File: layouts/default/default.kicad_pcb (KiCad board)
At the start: 2 copper layers, 38 x 75 mm, 52 parts, among them U2 LDO Vin max Iq, U3 LDO Vin max Iq

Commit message: do some layouts
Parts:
- removed C17: , atopile:C_0402_1005Metric
- added C13: 100nF ±10% 16V X7R, atopile:C0402-b3ef17, B.Cu at (0.00, 28.8)
- added C14: 100nF ±10% 16V X7R, atopile:C0402-b3ef17, B.Cu at (0.00, 33.8)
- added C15: 100nF ±10% 16V X7R, atopile:C0402-b3ef17, B.Cu at (0.00, 38.8)
- added C16: 100nF ±10% 16V X7R, atopile:C0402-b3ef17, B.Cu at (0.00, 47.9)
- added LED6: , atopile:LED-SMD_4P-L3.5-W2.8-BR-1-15b4e8, B.Cu at (0.00, 31.0)
- added LED7: , atopile:LED-SMD_4P-L3.5-W2.8-BR-1-15b4e8, B.Cu at (0.00, 36.0)
- added LED8: , atopile:LED-SMD_4P-L3.5-W2.8-BR-1-15b4e8, B.Cu at (0.00, 41.0)
- added LED9: , atopile:LED-SMD_4P-L3.5-W2.8-BR-1-15b4e8, B.Cu at (0.00, 46.0)
- C4, C5: value 100nF ±10% 50V X7R -> 20pF ±5% 50V C0G; footprint atopile:C0603-bd72f6 -> atopile:C0402-b3ef17
- Q1: footprint atopile:SOT-23-3_L2.9-W1.3-P1.90-LS2.4-BL-1-fcaf94 -> atopile:SOT-23-3_L2.9-W1.3-P1.90-LS2.4-BR-688f29
- R5: value 10kΩ ±1% 100mW -> 0Ω 100mW
- moved U4 36.5 mm to (-0.20, 43.5)
- moved S2 33.7 mm to (-21.1, 21.6), turned to -90 degrees
- moved R8 25.6 mm to (-18.7, 23.1)
- moved C1 24.2 mm to (-13.9, -8.60)
- moved C6 23.2 mm to (-17.1, 23.1)
- moved R7 22.1 mm to (-9.10, 9.60), turned to -90 degrees
- moved R12 19.6 mm to (17.6, 21.5), turned to -90 degrees
- moved C2 19.0 mm to (-15.5, 23.1), turned to -90 degrees
- moved S1 18.7 mm to (-11.5, 21.6)
- moved Q1 18.1 mm to (15.2, 22.2)
- moved FanConnector1 17.8 mm to (19.6, 18.4), turned to 90 degrees
- moved R3 16.7 mm to (-14.0, 23.1), turned to 90 degrees
- moved J2 14.7 mm to (17.6, 7.75), turned to 0 degrees
- moved D1 14.2 mm to (16.1, 18.4), turned to -90 degrees
- moved R13 12.7 mm to (14.4, 18.4), turned to -90 degrees
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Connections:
- net led_string-line-3 renamed led_string-line-8
- C1 pad 2: gnd -> gnd-1
- C10 pad 1: hv-3 -> hv
- C10 pad 2: gnd -> gnd-1
- C11 pad 1: hv-3 -> hv
- C11 pad 2: gnd -> gnd-1
- C12 pad 1: hv-3 -> hv
- C12 pad 2: gnd -> gnd-1
- C2 pad 1: mcu.mcu.boot_switch.lp_filter-line -> mcu.mcu-line
- C2 pad 2: mcu.mcu.boot_switch.lp_filter-gnd -> gnd-1
- C3 pad 1: hv -> hv-4
- C3 pad 2: gnd -> gnd-1
- C4 pad 2: gnd -> gnd-1
- C5 pad 1: mcu.mcu-line-1 -> mcu.mcu-line-2
- C5 pad 2: gnd -> gnd-1
- C6 pad 1: mcu.mcu.reset_switch.lp_filter-line -> line-1
- C6 pad 2: mcu.mcu.reset_switch.lp_filter-gnd -> gnd-1
- C7 pad 2: gnd -> gnd-1
- C8 pad 1: hv-3 -> hv
- C8 pad 2: gnd -> gnd-1
- C9 pad 1: hv-3 -> hv
- C9 pad 2: gnd -> gnd-1
- D1 pad 2: vindriktning_interface.fan_controller-gnd-1 -> vindriktning_interface.fan_controller-gnd
- FanConnector1 pad 1: vindriktning_interface.fan_controller-gnd-1 -> vindriktning_interface.fan_controller-gnd
- J1 pad 1: gnd -> gnd-1
- J1 pad 10: line-4 -> line
- J1 pad 11: line-3 -> line-6
- J1 pad 13: hv-1 -> hv-3
- J1 pad 14: gnd -> gnd-1
- J1 pad 2: hv-1 -> hv-3
- J1 pad 3: line-4 -> line
- J1 pad 4: line-3 -> line-6
- J1 pad 6: hv-1 -> hv-3
- J1 pad 7: gnd -> gnd-1
- J1 pad 8: gnd -> gnd-1
- J1 pad 9: hv-1 -> hv-3
- J2 pad 3: hv-3 -> hv
- J2 pad 4: gnd -> gnd-1
- LED1 pad 1: gnd -> gnd-1
- LED1 pad 3: hv-3 -> hv
- LED2 pad 1: gnd -> gnd-1
- LED2 pad 3: hv-3 -> hv
- LED2 pad 4: led_string-line-2 -> led_string-line-4
- LED3 pad 1: gnd -> gnd-1
- LED3 pad 2: led_string-line-2 -> led_string-line-4
- LED3 pad 3: hv-3 -> hv
- LED3 pad 4: led_string-line-4 -> led_string-line-5
- LED4 pad 1: gnd -> gnd-1
- LED4 pad 2: led_string-line-4 -> led_string-line-5
- LED4 pad 3: hv-3 -> hv
- LED5 pad 1: gnd -> gnd-1
- LED5 pad 3: hv-3 -> hv
- LED5 pad 4: led_string.leds[4]-line -> led_string-line-6
- Q1 pad 1: line-6 -> line-7
- Q1 pad 2: vindriktning_interface.fan_controller-gnd-1 -> vindriktning_interface.fan_controller-gnd
- Q1 pad 3: vindriktning_interface.fan_controller-gnd -> vindriktning_interface.fan_controller-gnd-1
- R1 pad 1: line-8 -> line-9
- R10 pad 2: gnd -> gnd-1
- R11 pad 2: gnd -> gnd-1
- R12 pad 1: line-6 -> line-7
- R12 pad 2: gnd -> gnd-1
- R13 pad 2: vindriktning_interface.fan_controller-gnd-1 -> vindriktning_interface.fan_controller-gnd
- R2 pad 1: line-5 -> line-10
- R3 pad 2: mcu.mcu.boot_switch.lp_filter-line -> mcu.mcu-line
- R4 pad 2: hv -> hv-4
- R5 pad 2: mcu.mcu-line-2 -> mcu.mcu-line-1
- R6 pad 1: line-8 -> line-9
- R6 pad 2: hv -> hv-4
- R7 pad 1: line-9 -> line-3
- R7 pad 2: hv -> hv-4
- R8 pad 2: mcu.mcu.reset_switch.lp_filter-line -> line-1
- R9 pad 2: gnd -> gnd-1
- S1 pad 3: gnd -> gnd-1
- S1 pad 4: gnd -> gnd-1
- S2 pad 3: gnd -> gnd-1
- S2 pad 4: gnd -> gnd-1
- U1 pad 10: line-5 -> line-10
- U1 pad 20: gnd -> gnd-1
- U1 pad 21: gnd -> gnd-1
- U1 pad 6: gnd -> gnd-1
- U1 pad 9: line-8 -> line-9
- U2 pad 1: hv-3 -> hv
- U2 pad 2: gnd -> gnd-1
- U2 pad 3: hv-3 -> hv
- U2 pad 5: hv -> hv-4
- U3 pad 1: hv-3 -> hv
- U3 pad 2: gnd -> gnd-1
- U3 pad 3: hv-3 -> hv
- U4 pad 2: lux_sensor.ic-line-1 -> lux_sensor.ic-line
- U4 pad 3: gnd -> gnd-1
- U4 pad 4: line-5 -> line-10
- U4 pad 5: lux_sensor.ic-line -> lux_sensor.ic-line-1
- U4 pad 6: line-8 -> line-9
- U5 pad 1: gnd -> gnd-1
- U5 pad 11: gnd -> gnd-1
- U5 pad 12: mcu.mcu-line-1 -> mcu.mcu-line-2
- U5 pad 13: mcu.mcu-line-2 -> mcu.mcu-line-1
- U5 pad 14: gnd -> gnd-1
- U5 pad 16: mcu.mcu.esp32_c3_mini_1.ic-line -> mcu.mcu.esp32_c3_mini_1.ic-line-1
- U5 pad 18: line-6 -> line-7
- U5 pad 19: line-7 -> line-8
- U5 pad 2: gnd -> gnd-1
- U5 pad 20: line-10 -> line-5
- U5 pad 21: mcu.mcu.esp32_c3_mini_1.ic-line-1 -> mcu.mcu.esp32_c3_mini_1.ic-line
- U5 pad 22: line-9 -> line-3
- U5 pad 26: line-4 -> line
- U5 pad 27: line-3 -> line-6
- U5 pad 3: hv -> hv-4
- U5 pad 30: line -> line-2
- U5 pad 31: line-2 -> line-4
- U5 pad 36: gnd -> gnd-1
- U5 pad 37: gnd -> gnd-1
- U5 pad 38: gnd -> gnd-1
- U5 pad 39: gnd -> gnd-1
- U5 pad 40: gnd -> gnd-1
- U5 pad 41: gnd -> gnd-1
- U5 pad 42: gnd -> gnd-1
- U5 pad 43: gnd -> gnd-1
- U5 pad 44: gnd -> gnd-1
- U5 pad 45: gnd -> gnd-1
- U5 pad 46: gnd -> gnd-1
- U5 pad 47: gnd -> gnd-1
- U5 pad 48: gnd -> gnd-1
- U5 pad 49: gnd -> gnd-1
- U5 pad 5: line-8 -> line-9
- U5 pad 50: gnd -> gnd-1
- U5 pad 51: gnd -> gnd-1
- U5 pad 52: gnd -> gnd-1
- U5 pad 53: gnd -> gnd-1
- U5 pad 54: gnd -> gnd-1
- U5 pad 55: gnd -> gnd-1
- U5 pad 56: gnd -> gnd-1
- U5 pad 57: gnd -> gnd-1
- U5 pad 58: gnd -> gnd-1
- U5 pad 59: gnd -> gnd-1
- U5 pad 6: line-5 -> line-10
- U5 pad 60: gnd -> gnd-1
- U5 pad 61: gnd -> gnd-1
- U6 pad 2: gnd -> gnd-1
- U6 pad 5: line-9 -> line-3
- U6 pad 7: hv-3 -> hv
- U7 pad 1: line-10 -> line-5
- U7 pad 2: line-2 -> line-4
- U7 pad 3: line -> line-2
- U7 pad 4: gnd -> gnd-1
- U7 pad 5: hv-3 -> hv
- U8 pad 2: gnd -> gnd-1
- U8 pad 5: line-7 -> line-8
- U8 pad 7: hv-3 -> hv
- X1 pad 1: gnd-1 -> gnd
- X1 pad 2: hv-4 -> hv-1
- X1 pad 3: line-5 -> line-10
- X1 pad 4: line-8 -> line-9
- XTAL1 pad 2: mcu.mcu-line-1 -> mcu.mcu-line-2
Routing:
- net hv: track 0.00 -> 72.5 mm, vias 0 -> 2
- net (no net): track 38.0 -> 0.00 mm
- net gnd: track 36.7 -> 0.00 mm
- net led_string-line-4: track 38.0 -> 5.42 mm
- net hv-3: track 31.4 -> 0.00 mm, vias 4 -> 0
- net gnd-1: track 0.00 -> 26.9 mm, vias 0 -> 21
- net line-1: track 2.41 -> 22.1 mm
- net vindriktning_interface-line: track 22.3 -> 5.32 mm
- net vindriktning_interface-line-1: track 18.7 -> 5.39 mm
- net vindriktning_interface.fan_controller-gnd-1: track 13.1 -> 1.10 mm, vias 0 -> 1
- net mount[1]: track 10.9 -> 0.00 mm, vias 0 -> 37
- net led_string-line-3: track 0.00 -> 10.5 mm
- net led_string.leds[4]-line: track 9.81 -> 0.00 mm
- net co2_sensor.footprint.pins[19].net-net: track 9.81 -> 0.00 mm
- net cc1: track 9.81 -> 0.00 mm
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- added copper zone on F.Cu, net gnd-1
- added copper zone on In1.Cu, net gnd-1
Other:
- board size 38 x 75 mm -> 46 x 75 mm
- copper layers 2 -> 4
- board text removed: "069b639"
- board text removed: "325bd98"
- board text removed: "380a7ca"
- board text removed: "Vindriktning"
- board text removed: "a4eeddd"
- board text removed: "d9546bd"

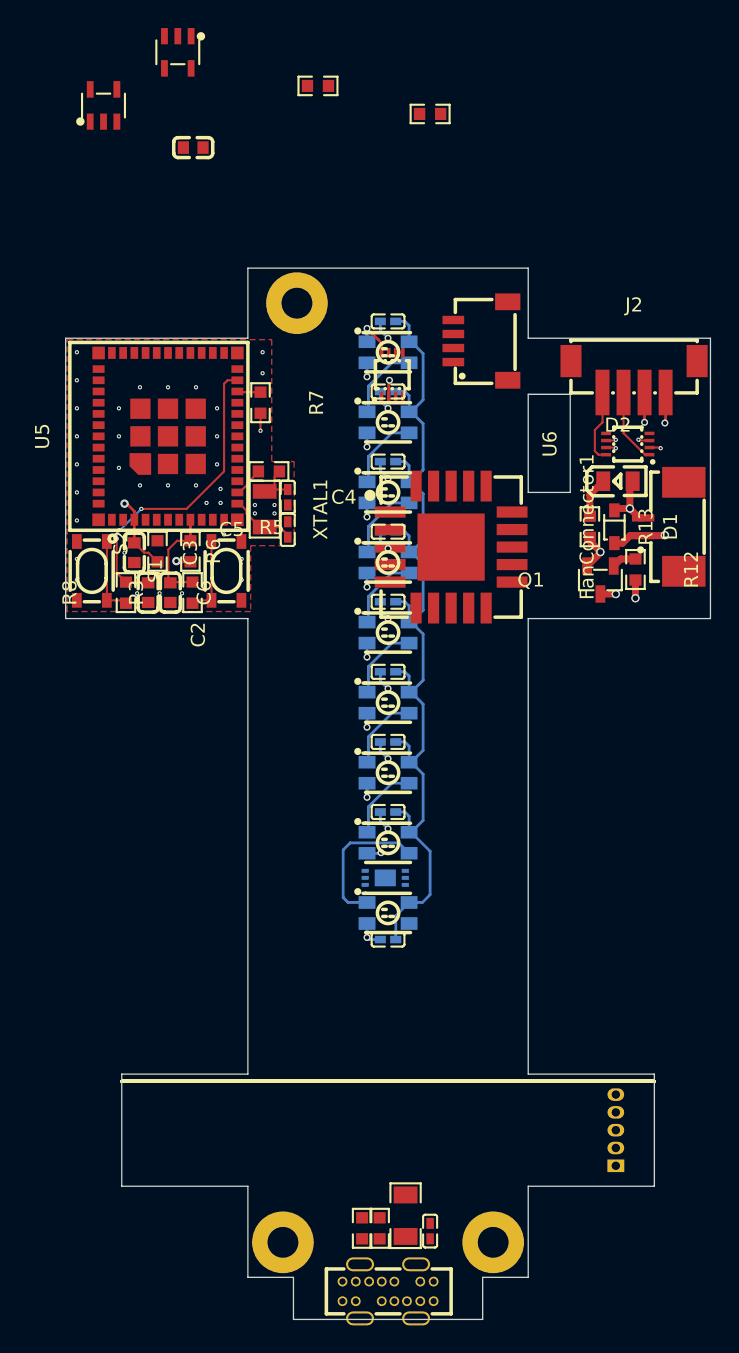
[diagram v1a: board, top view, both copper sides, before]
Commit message: Try to fix fuses
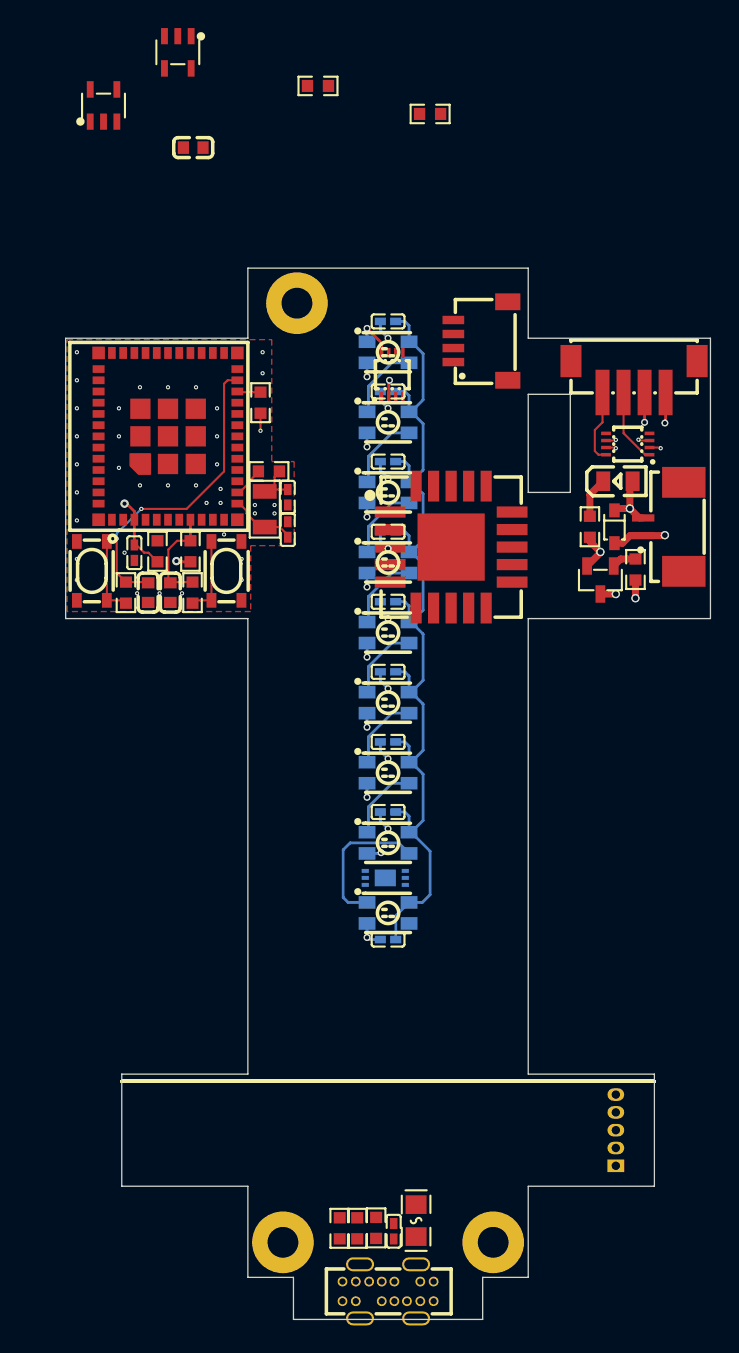
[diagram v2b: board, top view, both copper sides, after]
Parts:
- added F1: , atopile:F0805-d5954a, F.Cu at (2.00, 68.0)
- C3: value 1µF ±10% 50V X5R -> 1µF ±10% 25V X5R; footprint atopile:C0603-bd72f6 -> atopile:C0402-b3ef17
- R11: value 1MΩ ±1% 250mW -> 1MΩ ±1% 100mW; footprint atopile:R1206-bdb864 -> atopile:R0603-ebcab9
- moved C7 2.60 mm to (0.40, 68.7)
- moved R11 2.27 mm to (-0.85, 68.5)
- moved R10 1.60 mm to (-2.20, 68.5)
- moved R9 1.60 mm to (-3.45, 68.5)
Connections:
- C1 pad 2: gnd-1 -> gnd
- C10 pad 2: gnd-1 -> gnd
- C11 pad 2: gnd-1 -> gnd
- C12 pad 2: gnd-1 -> gnd
- C13 pad 2: gnd-1 -> gnd
- C14 pad 2: gnd-1 -> gnd
- C15 pad 2: gnd-1 -> gnd
- C16 pad 2: gnd-1 -> gnd
- C2 pad 2: gnd-1 -> gnd
- C3 pad 1: hv-4 -> hv-1
- C3 pad 2: gnd-1 -> gnd
- C4 pad 2: gnd-1 -> gnd
- C5 pad 2: gnd-1 -> gnd
- C6 pad 1: line-1 -> line-4
- C6 pad 2: gnd-1 -> gnd
- C7 pad 2: gnd-1 -> gnd
- C8 pad 2: gnd-1 -> gnd
- C9 pad 2: gnd-1 -> gnd
- D1 pad 2: vindriktning_interface.fan_controller-gnd -> vindriktning_interface.fan_controller-gnd-1
- FanConnector1 pad 1: vindriktning_interface.fan_controller-gnd -> vindriktning_interface.fan_controller-gnd-1
- J1 pad 1: gnd-1 -> gnd
- J1 pad 11: line-6 -> line-3
- J1 pad 13: hv-3 -> usb_psu-hv
- J1 pad 14: gnd-1 -> gnd
- J1 pad 2: hv-3 -> usb_psu-hv
- J1 pad 4: line-6 -> line-3
- J1 pad 6: hv-3 -> usb_psu-hv
- J1 pad 7: gnd-1 -> gnd
- J1 pad 8: gnd-1 -> gnd
- J1 pad 9: hv-3 -> usb_psu-hv
- J2 pad 4: gnd-1 -> gnd
- LED1 pad 1: gnd-1 -> gnd
- LED1 pad 2: led_string-line-8 -> led_string-line
- LED1 pad 4: led_string-line -> led_string-line-7
- LED2 pad 1: gnd-1 -> gnd
- LED2 pad 2: led_string-line -> led_string-line-7
- LED2 pad 4: led_string-line-4 -> led_string-line-1
- LED3 pad 1: gnd-1 -> gnd
- LED3 pad 2: led_string-line-4 -> led_string-line-1
- LED3 pad 4: led_string-line-5 -> led_string-line-8
- LED4 pad 1: gnd-1 -> gnd
- LED4 pad 2: led_string-line-5 -> led_string-line-8
- LED4 pad 4: led_string-line-1 -> led_string-line-4
- LED5 pad 1: gnd-1 -> gnd
- LED5 pad 2: led_string-line-1 -> led_string-line-4
- LED5 pad 4: led_string-line-6 -> led_string-line-5
- LED6 pad 1: gnd-1 -> gnd
- LED6 pad 2: led_string-line-6 -> led_string-line-5
- LED6 pad 4: led_string-line-2 -> led_string-line-6
- LED7 pad 1: gnd-1 -> gnd
- LED7 pad 2: led_string-line-2 -> led_string-line-6
- LED7 pad 4: led_string-line-7 -> led_string-line-3
- LED8 pad 1: gnd-1 -> gnd
- LED8 pad 2: led_string-line-7 -> led_string-line-3
- LED8 pad 4: led_string-line-3 -> led_string-line-2
- LED9 pad 1: gnd-1 -> gnd
- LED9 pad 2: led_string-line-3 -> led_string-line-2
- Q1 pad 2: vindriktning_interface.fan_controller-gnd -> vindriktning_interface.fan_controller-gnd-1
- Q1 pad 3: vindriktning_interface.fan_controller-gnd-1 -> vindriktning_interface.fan_controller-gnd
- R10 pad 2: gnd-1 -> gnd
- R11 pad 2: gnd-1 -> gnd
- R12 pad 2: gnd-1 -> gnd
- R13 pad 2: vindriktning_interface.fan_controller-gnd -> vindriktning_interface.fan_controller-gnd-1
- R2 pad 1: line-10 -> line-2
- R4 pad 2: hv-4 -> hv-1
- R6 pad 2: hv-4 -> hv-1
- R7 pad 1: line-3 -> line-1
- R7 pad 2: hv-4 -> hv-1
- R8 pad 2: line-1 -> line-4
- R9 pad 2: gnd-1 -> gnd
- S1 pad 3: gnd-1 -> gnd
- S1 pad 4: gnd-1 -> gnd
- S2 pad 3: gnd-1 -> gnd
- S2 pad 4: gnd-1 -> gnd
- U1 pad 10: line-10 -> line-2
- U1 pad 20: gnd-1 -> gnd
- U1 pad 21: gnd-1 -> gnd
- U1 pad 6: gnd-1 -> gnd
- U2 pad 2: gnd-1 -> gnd
- U2 pad 5: hv-4 -> hv-1
- U3 pad 2: gnd-1 -> gnd
- U4 pad 2: lux_sensor.ic-line -> lux_sensor.ic-line-1
- U4 pad 3: gnd-1 -> gnd
- U4 pad 4: line-10 -> line-2
- U4 pad 5: lux_sensor.ic-line-1 -> lux_sensor.ic-line-2
- U4 pad 7: lux_sensor.ic-line-2 -> lux_sensor.ic-line
- U5 pad 1: gnd-1 -> gnd
- U5 pad 11: gnd-1 -> gnd
- U5 pad 14: gnd-1 -> gnd
- U5 pad 16: mcu.mcu.esp32_c3_mini_1.ic-line-1 -> mcu.mcu.esp32_c3_mini_1.ic-line
- U5 pad 19: line-8 -> line-10
- U5 pad 2: gnd-1 -> gnd
- U5 pad 20: line-5 -> line-6
- U5 pad 21: mcu.mcu.esp32_c3_mini_1.ic-line -> mcu.mcu.esp32_c3_mini_1.ic-line-1
- U5 pad 22: line-3 -> line-1
- U5 pad 23: line-1 -> line-4
- U5 pad 27: line-6 -> line-3
- U5 pad 3: hv-4 -> hv-1
- U5 pad 30: line-2 -> line-8
- U5 pad 31: line-4 -> line-5
- U5 pad 36: gnd-1 -> gnd
- U5 pad 37: gnd-1 -> gnd
- U5 pad 38: gnd-1 -> gnd
- U5 pad 39: gnd-1 -> gnd
- U5 pad 40: gnd-1 -> gnd
- U5 pad 41: gnd-1 -> gnd
- U5 pad 42: gnd-1 -> gnd
- U5 pad 43: gnd-1 -> gnd
- U5 pad 44: gnd-1 -> gnd
- U5 pad 45: gnd-1 -> gnd
- U5 pad 46: gnd-1 -> gnd
- U5 pad 47: gnd-1 -> gnd
- U5 pad 48: gnd-1 -> gnd
- U5 pad 49: gnd-1 -> gnd
- U5 pad 50: gnd-1 -> gnd
- U5 pad 51: gnd-1 -> gnd
- U5 pad 52: gnd-1 -> gnd
- U5 pad 53: gnd-1 -> gnd
- U5 pad 54: gnd-1 -> gnd
- U5 pad 55: gnd-1 -> gnd
- U5 pad 56: gnd-1 -> gnd
- U5 pad 57: gnd-1 -> gnd
- U5 pad 58: gnd-1 -> gnd
- U5 pad 59: gnd-1 -> gnd
- U5 pad 6: line-10 -> line-2
- U5 pad 60: gnd-1 -> gnd
- U5 pad 61: gnd-1 -> gnd
- U6 pad 2: gnd-1 -> gnd
- U6 pad 4: line-1 -> line-4
- U6 pad 5: line-3 -> line-1
- U7 pad 1: line-5 -> line-6
- U7 pad 2: line-4 -> line-5
- U7 pad 3: line-2 -> line-8
- U7 pad 4: gnd-1 -> gnd
- U8 pad 2: gnd-1 -> gnd
- U8 pad 5: line-8 -> line-10
- U8 pad 8: led_string-line-8 -> led_string-line
- X1 pad 1: gnd -> gnd-1
- X1 pad 2: hv-1 -> hv-3
- X1 pad 3: line-10 -> line-2
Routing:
- net gnd-1: track 26.9 -> 0.00 mm, vias 21 -> 0
- net gnd: track 0.00 -> 26.9 mm, vias 0 -> 21
- net line-4: track 0.00 -> 22.1 mm, vias 0 -> 2
- net line-1: track 22.1 -> 1.67 mm, vias 2 -> 0
- net hv-4: track 7.66 -> 0.00 mm, vias 3 -> 0
- net hv-1: track 0.00 -> 7.66 mm, vias 0 -> 3
- net vindriktning_interface.fan_controller-gnd-1: track 1.10 -> 6.66 mm, vias 1 -> 2
- net vindriktning_interface.fan_controller-gnd: track 6.66 -> 1.10 mm, vias 2 -> 1
- net led_string-line-3: track 10.5 -> 5.42 mm
- net led_string-line-2: track 5.42 -> 10.5 mm
- net led_string-line-8: track 3.13 -> 5.42 mm, vias 1 -> 0
- net led_string-line: track 5.42 -> 3.13 mm, vias 0 -> 1
- net line-3: track 1.67 -> 0.00 mm
- added copper zone on F.Cu, net gnd
- added copper zone on In1.Cu, net gnd
- added copper zone on In2.Cu, net hv
- removed copper zone on F.Cu, net gnd-1
- removed copper zone on In1.Cu, net gnd-1
